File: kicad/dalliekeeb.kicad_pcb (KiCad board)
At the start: 2 copper layers, 124.2 x 100.8 mm, 61 parts

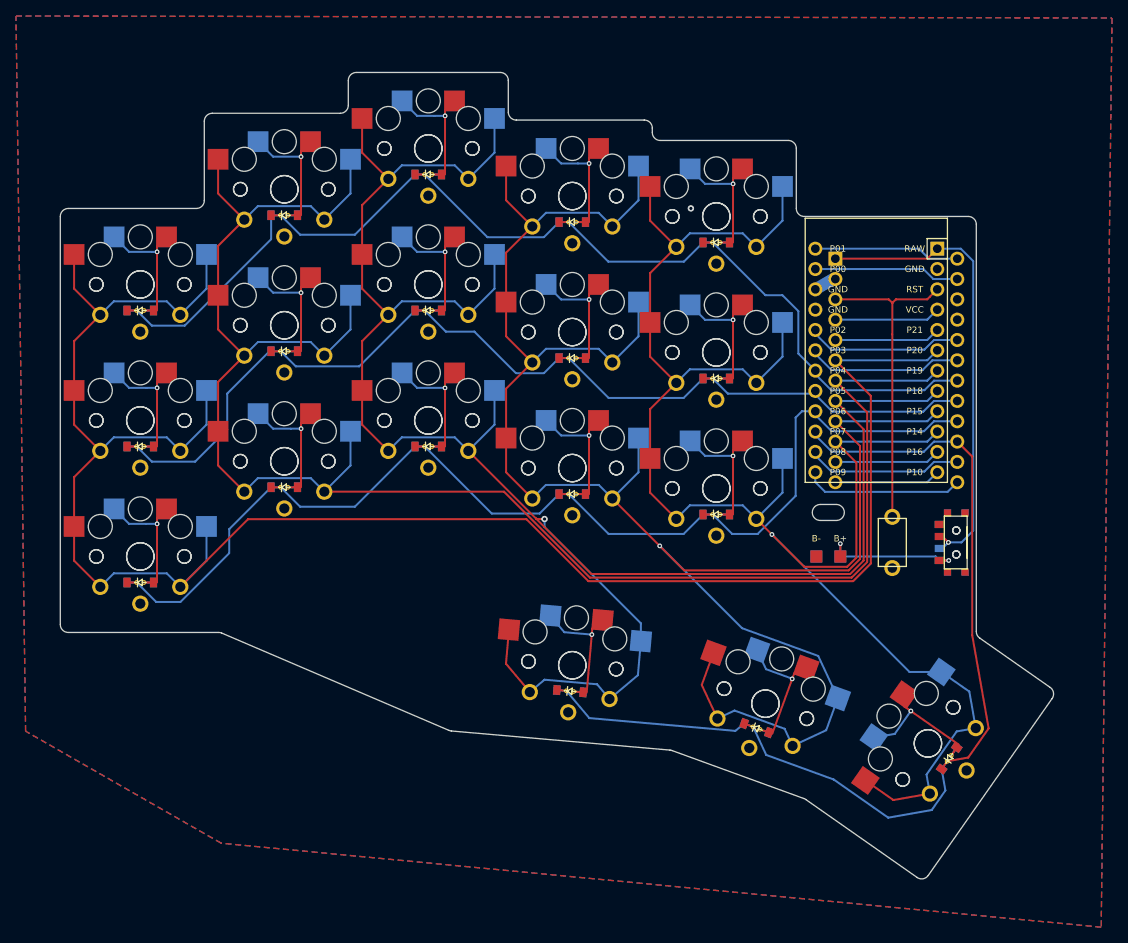
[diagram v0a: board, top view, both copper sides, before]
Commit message: Cleanup traces and make ✨curvy✨
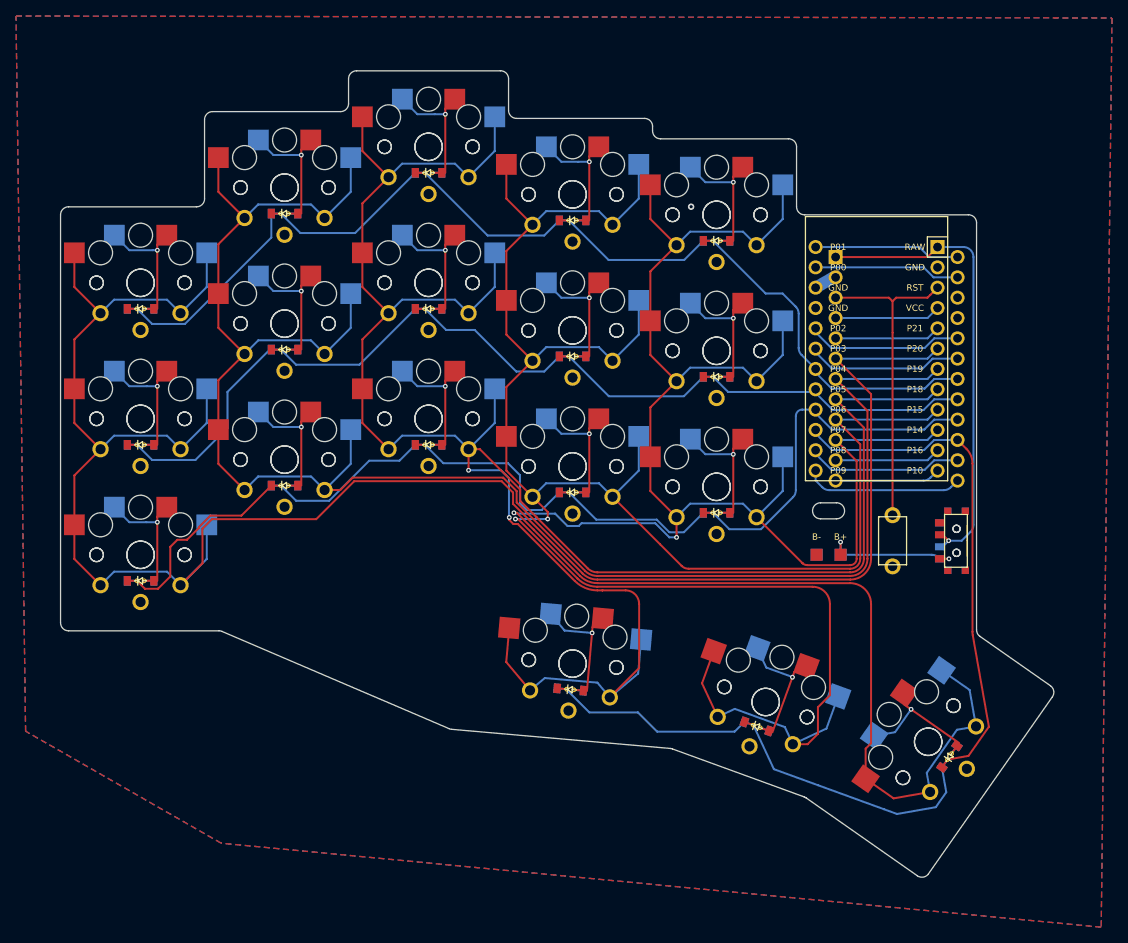
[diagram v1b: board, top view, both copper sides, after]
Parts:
- moved MCU1 0.21 mm to (231.1, 81.1)
- moved S5 0.21 mm to (139.1, 71.6)
- moved S6 0.21 mm to (139.1, 71.6)
- moved D12 0.21 mm to (193.1, 63.8)
- moved S17 0.21 mm to (175.1, 54.6)
- moved S18 0.21 mm to (175.1, 54.6)
- moved D6 0.21 mm to (157.1, 62.9)
- moved D3 0.21 mm to (139.1, 74.8)
- moved S25 0.21 mm to (211.1, 97.1)
- moved S26 0.21 mm to (211.1, 97.1)
- moved S21 0.21 mm to (193.1, 77.5)
- moved S22 0.21 mm to (193.1, 77.5)
- moved S3 0.21 mm to (139.1, 88.6)
- moved S4 0.21 mm to (139.1, 88.6)
- moved S1 0.21 mm to (139.1, 105.6)
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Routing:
- net P14: track 211.1 -> 279.1 mm, vias 1 -> 2
- net P15: track 236.0 -> 277.6 mm, vias 1 -> 2
- net P18: track 251.0 -> 277.8 mm, vias 1 -> 2
- net P20: track 243.7 -> 250.8 mm
- net P19: track 220.0 -> 222.1 mm
- net P7: track 127.3 -> 128.3 mm

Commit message: Add pcb art
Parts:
- added G***: LOGO, libs:dusk, F.Cu at (166.4, 111.6)
- added G***: LOGO, libs:dusk, B.Cu at (166.4, 111.6)
